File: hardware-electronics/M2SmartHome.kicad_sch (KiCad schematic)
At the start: 5 parts, among them J1 M.2-Key-M-edge-connector

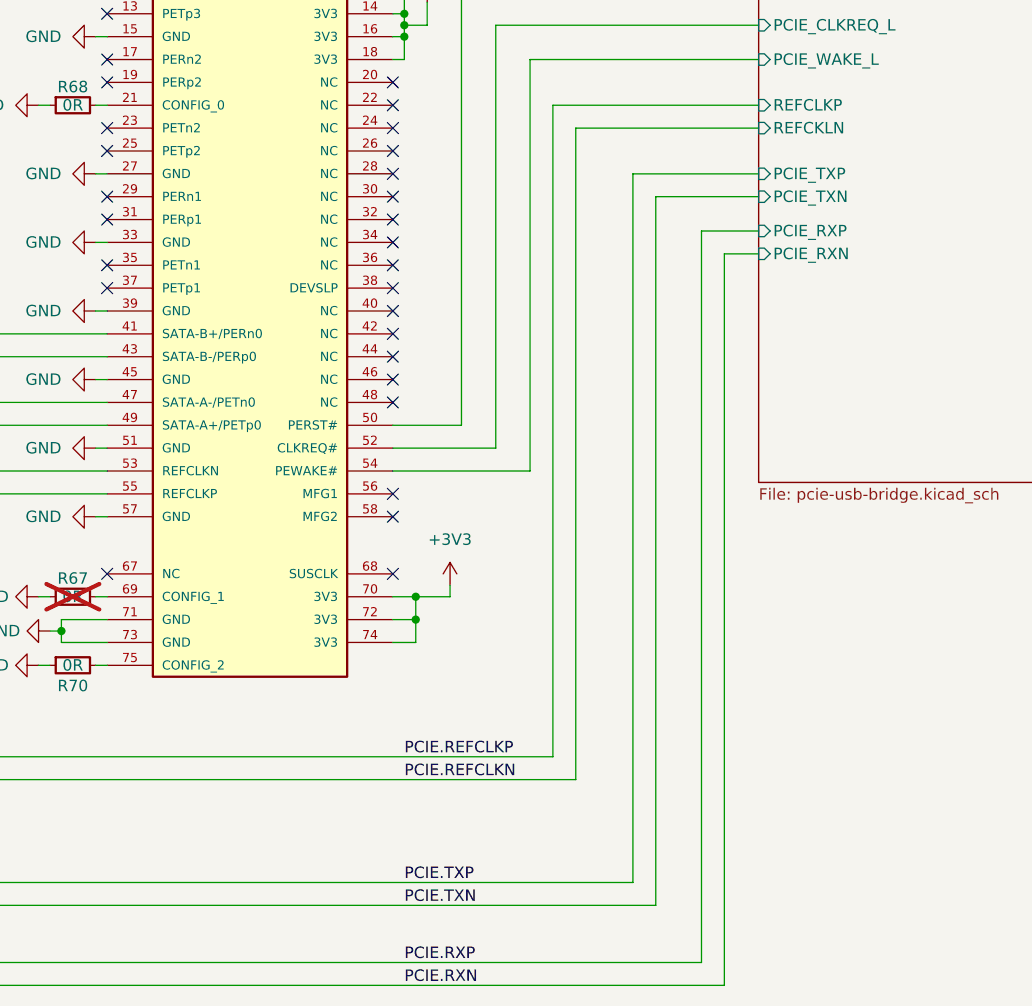
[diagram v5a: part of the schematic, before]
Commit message: [#26] Correct TX/RX PCIe line swap
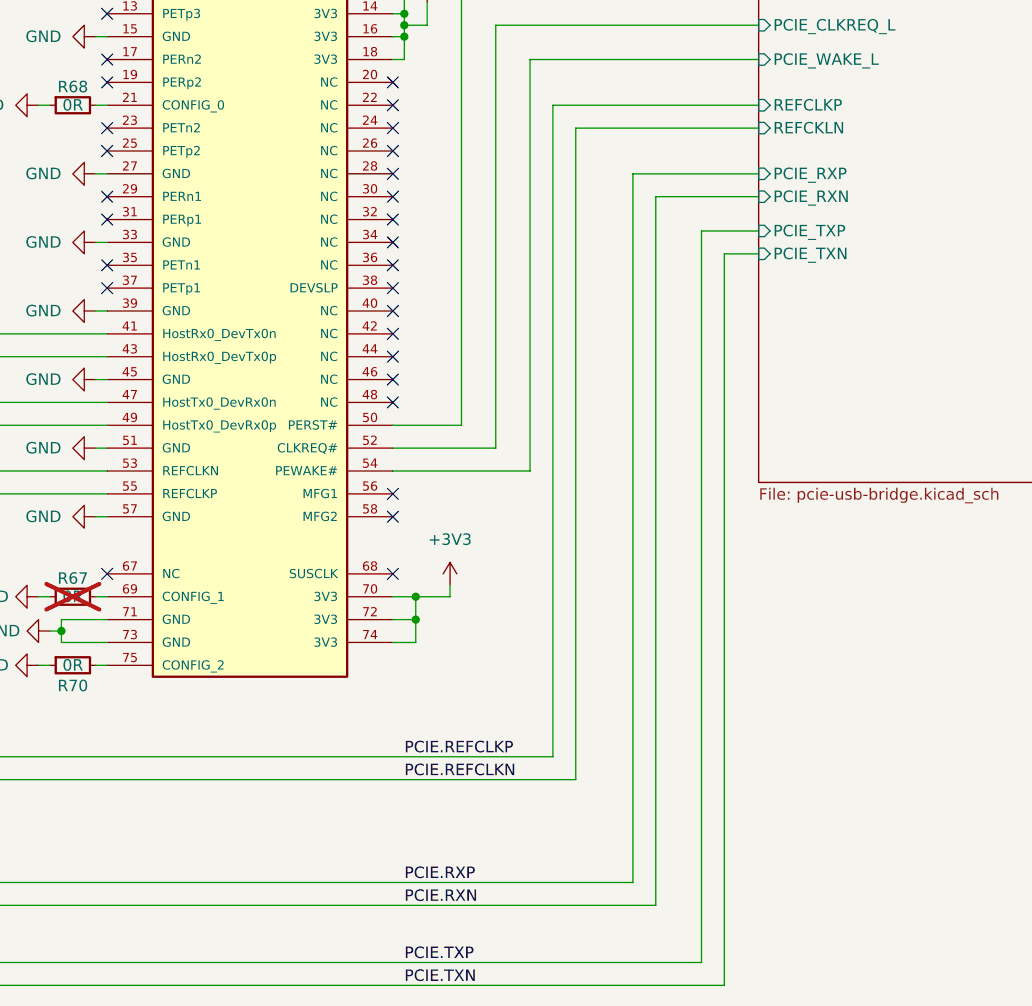
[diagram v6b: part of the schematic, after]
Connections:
- net PCIE.RXN: now also J1.47 (HostTx0_DevRx0n); no longer J1.41 (SATA-B+/PERn0)
- net PCIE.RXP: now also J1.49 (HostTx0_DevRx0p); no longer J1.43 (SATA-B-/PERp0)
- net PCIE.TXN: now also J1.41 (HostRx0_DevTx0n); no longer J1.47 (SATA-A-/PETn0)
- net PCIE.TXP: now also J1.43 (HostRx0_DevTx0p); no longer J1.49 (SATA-A+/PETp0)
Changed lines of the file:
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@@
 	(wire
 		(pts
-			(xy 96.52 67.31) (xy 97.79 67.31)
+			(xy 170.18 81.28) (xy 176.53 81.28)
 		)
 		(stroke
@@
 	(wire
 		(pts
-			(xy 172.72 83.82) (xy 176.53 83.82)
+			(xy 96.52 67.31) (xy 97.79 67.31)
 		)
 		(stroke
@@
 	(wire
 		(pts
+			(xy 165.1 77.47) (xy 176.53 77.47)
+		)
+		(stroke
+			(width 0)
+			(type default)
+		)
+	)
+	(wire
+		(pts
 			(xy 102.87 105.41) (xy 104.14 105.41)
 		)
@@
 	(wire
 		(pts
-			(xy 176.53 77.47) (xy 165.1 77.47)
-		)
-		(stroke
-			(width 0)
-			(type default)
-		)
-	)
-	(wire
-		(pts
 			(xy 297.18 105.41) (xy 267.97 105.41)
 		)
@@
 	(wire
 		(pts
-			(xy 232.41 74.93) (xy 267.97 74.93)
+			(xy 172.72 83.82) (xy 176.53 83.82)
 		)
 		(stroke
@@
 	(wire
 		(pts
-			(xy 165.1 77.47) (xy 165.1 156.21)
+			(xy 232.41 74.93) (xy 267.97 74.93)
 		)
 		(stroke
@@
 	(wire
 		(pts
-			(xy 176.53 81.28) (xy 170.18 81.28)
+			(xy 165.1 77.47) (xy 165.1 156.21)
 		)
 		(stroke
@@
 	(wire
 		(pts
-			(xy 162.56 74.93) (xy 176.53 74.93)
-		)
-		(stroke
-			(width 0)
-			(type default)
-		)
-	)
-	(wire
-		(pts
 			(xy 176.53 67.31) (xy 153.67 67.31)
 		)
@@
 	(wire
 		(pts
+			(xy 162.56 74.93) (xy 176.53 74.93)
+		)
+		(stroke
+			(width 0)
+			(type default)
+		)
+	)
+	(wire
+		(pts
 			(xy 97.79 125.73) (xy 99.06 125.73)
 		)
@@
 		)
 	)
-	(label "PCIE.REFCLKP"
-		(at 137.16 139.7 0)
+	(label "PCIE.TXP"
+		(at 137.16 162.56 0)
 		(fields_autoplaced yes)
 		(effects
@@
 		)
 	)
-	(label "PCIE.TXN"
-		(at 137.16 156.21 0)
+	(label "PCIE.RXP"
+		(at 137.16 153.67 0)
 		(fields_autoplaced yes)
 		(effects
@@
 	)
 	(label "PCIE.RXN"
-		(at 137.16 165.1 0)
+		(at 137.16 156.21 0)
 		(fields_autoplaced yes)
 		(effects
@@
 		)
 	)
-	(label "PCIE.RXP"
-		(at 137.16 162.56 0)
+	(label "PCIE.REFCLKP"
+		(at 137.16 139.7 0)
 		(fields_autoplaced yes)
 		(effects
@@
 		)
 	)
-	(label "PCIE.TXP"
-		(at 137.16 153.67 0)
+	(label "PCIE.TXN"
+		(at 137.16 165.1 0)
 		(fields_autoplaced yes)
 		(effects
@@
 		)
 		(pin "PCIE_RXN" input
-			(at 176.53 83.82 180)
+			(at 176.53 77.47 180)
 			(effects
 				(font
@@
 		)
 		(pin "PCIE_RXP" input
-			(at 176.53 81.28 180)
+			(at 176.53 74.93 180)
 			(effects
 				(font
@@
 		)
 		(pin "PCIE_TXP" input
-			(at 176.53 74.93 180)
+			(at 176.53 81.28 180)
 			(effects
 				(font
@@
 		)
 		(pin "PCIE_TXN" input
-			(at 176.53 77.47 180)
+			(at 176.53 83.82 180)
 			(effects
 				(font

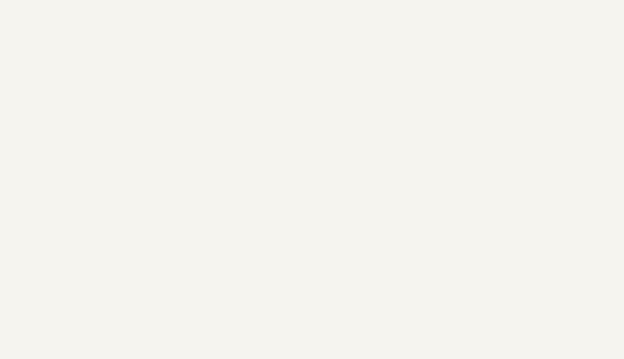
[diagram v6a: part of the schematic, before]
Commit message: [#26] PCB improve RBias routing
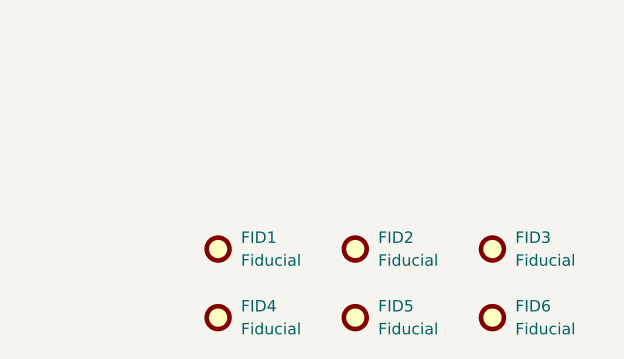
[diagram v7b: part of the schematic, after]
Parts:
- added FID1, FID2, FID3, FID4, FID5, FID6: Fiducial, Fiducial:Fiducial_0.5mm_Mask1mm, symbol Mechanical:Fiducial

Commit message: M.2-Key-M-edge-connector exclude from BOM
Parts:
- J1: now left out of the parts list
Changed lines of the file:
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@@
 		(unit 1)
 		(exclude_from_sim no)
-		(in_bom yes)
+		(in_bom no)
 		(on_board yes)
 		(dnp no)
